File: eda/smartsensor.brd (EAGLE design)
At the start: 33 x 27.9 mm, 19 parts, among them IC1 FT232RL, IC2 ATMEGA32U4-AU

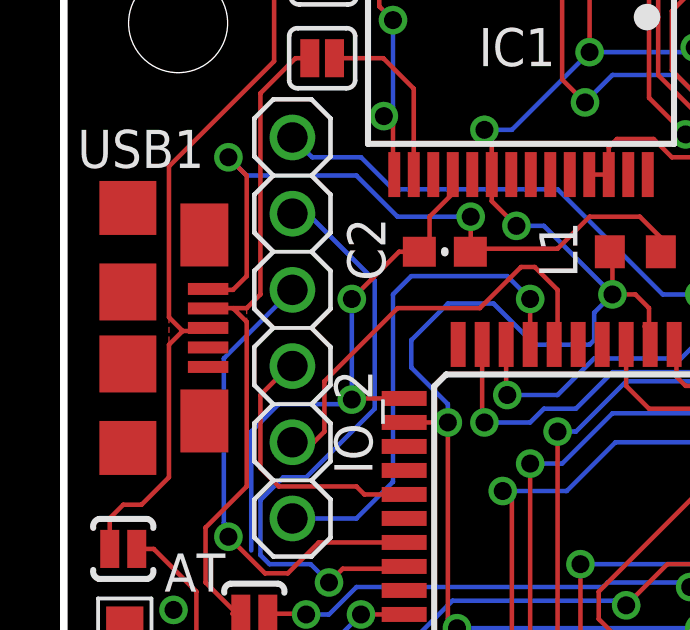
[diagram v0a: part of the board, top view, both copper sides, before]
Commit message: Fix ground plane clearance on smartsensor
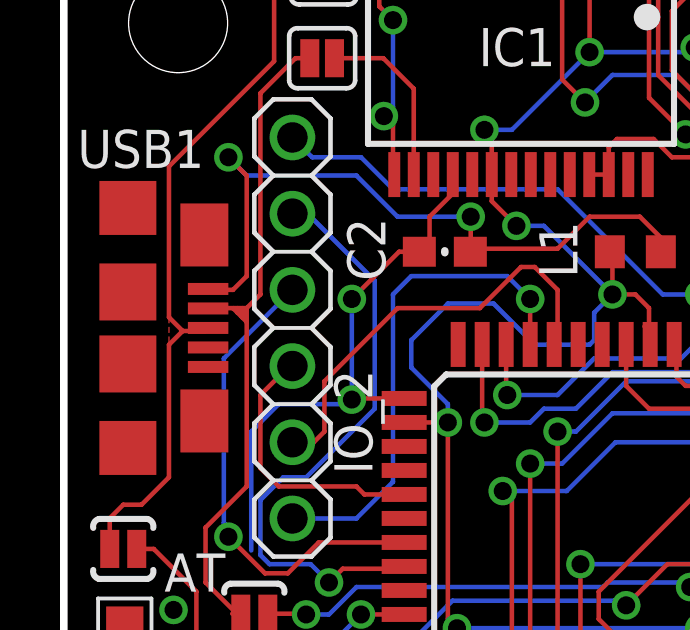
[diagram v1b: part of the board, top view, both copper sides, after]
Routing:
- net D-: track 22.7 -> 23.6 mm
- removed copper zone on layer 1, net D-
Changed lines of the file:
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@@
 <contactref element="USB1" pad="P$7"/>
 <contactref element="USB1" pad="P$9"/>
-<wire x1="4.685" y1="10.87" x2="6.2484" y2="10.5156" width="0" layer="19" extent="1-16"/>
-<wire x1="2.135" y1="12.77" x2="4.81" y2="12.67" width="0" layer="19" extent="1-1"/>
+<wire x1="4.81" y1="12.67" x2="2.135" y2="12.77" width="0" layer="19" extent="1-1"/>
+<wire x1="6.2484" y1="10.5156" x2="4.685" y2="10.87" width="0" layer="19" extent="1-16"/>
 <wire x1="4.685" y1="17.07" x2="2.135" y2="17.97" width="0" layer="19" extent="1-1"/>
-<wire x1="3.6576" y1="4.572" x2="6.2484" y2="6.5532" width="0" layer="19" extent="1-16"/>
-<wire x1="2.159" y1="3.9624" x2="3.6576" y2="4.572" width="0" layer="19" extent="1-16"/>
+<wire x1="3.6576" y1="4.572" x2="6.2484" y2="6.5532" width="0" layer="19" extent="16-16"/>
 </signal>
 <signal name="RX">
@@
 <wire x1="5.9" y1="4.445" x2="5.6134" y2="4.445" width="0.1524" layer="1"/>
 <wire x1="6.096" y1="8.6868" x2="6.096" y2="14.1732" width="0.1524" layer="1"/>
-<wire x1="6.096" y1="14.1732" x2="5.6388" y2="14.6304" width="0.1524" layer="1"/>
+<wire x1="6.096" y1="14.1732" x2="5.9436" y2="14.3256" width="0.1524" layer="1"/>
+<wire x1="5.7912" y1="14.478" x2="5.6388" y2="14.6304" width="0.1524" layer="1"/>
 <wire x1="4.81" y1="14.62" x2="4.8204" y2="14.6304" width="0.1524" layer="1"/>
 <wire x1="4.8204" y1="14.6304" x2="5.6388" y2="14.6304" width="0.1524" layer="1"/>
-<wire x1="5.6388" y1="14.6304" x2="6.096" y2="14.6304" width="0.1524" layer="1"/>
+<wire x1="5.6388" y1="14.6304" x2="5.7912" y2="14.6304" width="0.1524" layer="1"/>
+<wire x1="5.7912" y1="14.6304" x2="5.9436" y2="14.6304" width="0.1524" layer="1"/>
 <wire x1="6.096" y1="14.6304" x2="6.5532" y2="15.0876" width="0.1524" layer="1"/>
 <wire x1="6.5532" y1="15.0876" x2="6.5532" y2="21.7932" width="0.1524" layer="1"/>
@@
 <wire x1="4.7244" y1="5.4864" x2="5.7658" y2="4.445" width="0.1524" layer="1"/>
 <wire x1="5.7658" y1="4.445" x2="5.9" y2="4.445" width="0.1524" layer="1"/>
-<polygon width="0.1524" layer="1">
-<vertex x="5.6388" y="14.6304"/>
-<vertex x="6.096" y="14.6304"/>
-<vertex x="6.096" y="14.1732"/>
-</polygon>
 <wire x1="8.0971" y1="22.86" x2="8.1987" y2="22.9616" width="0.1524" layer="1"/>
 <wire x1="6.5532" y1="21.7932" x2="7.7216" y2="22.9616" width="0.1524" layer="1"/>
 <wire x1="7.7216" y1="22.9616" x2="8.1987" y2="22.9616" width="0.1524" layer="1"/>
+<wire x1="6.096" y1="14.1732" x2="6.096" y2="14.6304" width="0.1524" layer="1"/>
+<wire x1="6.096" y1="14.6304" x2="5.9436" y2="14.6304" width="0.1524" layer="1"/>
+<wire x1="5.9436" y1="14.6304" x2="5.9436" y2="14.3256" width="0.1524" layer="1"/>
+<wire x1="5.9436" y1="14.3256" x2="5.7912" y2="14.478" width="0.1524" layer="1"/>
+<wire x1="5.7912" y1="14.478" x2="5.7912" y2="14.6304" width="0.1524" layer="1"/>
 </signal>
 <signal name="D+">
@@
 </signal>
 </signals>
-<errors>
-</errors>
 </board>
 </drawing>
